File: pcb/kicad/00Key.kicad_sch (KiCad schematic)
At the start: 4 parts

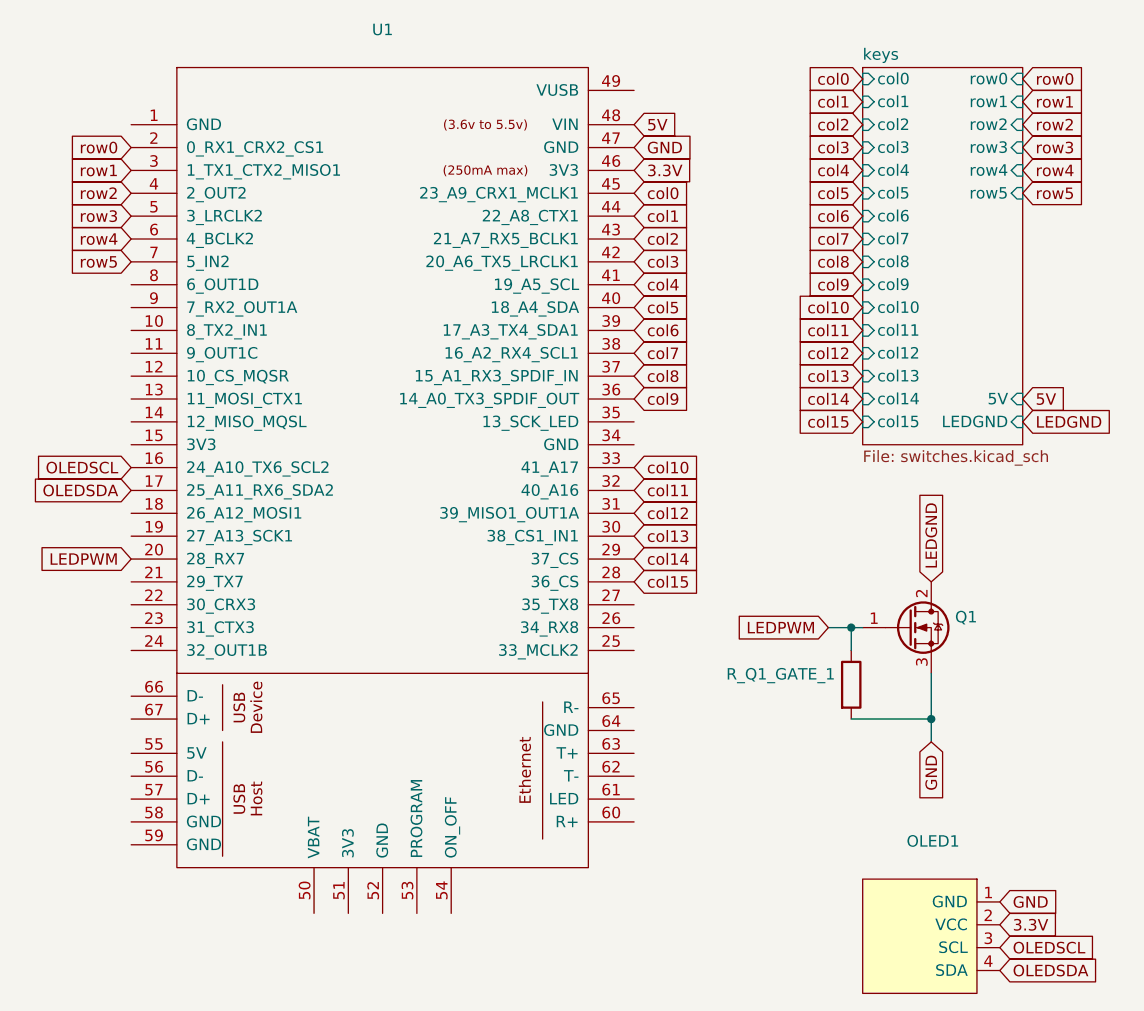
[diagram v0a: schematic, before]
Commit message: Modified schematic and pcb to use kailh hotswaps rather than MX+LED footprints
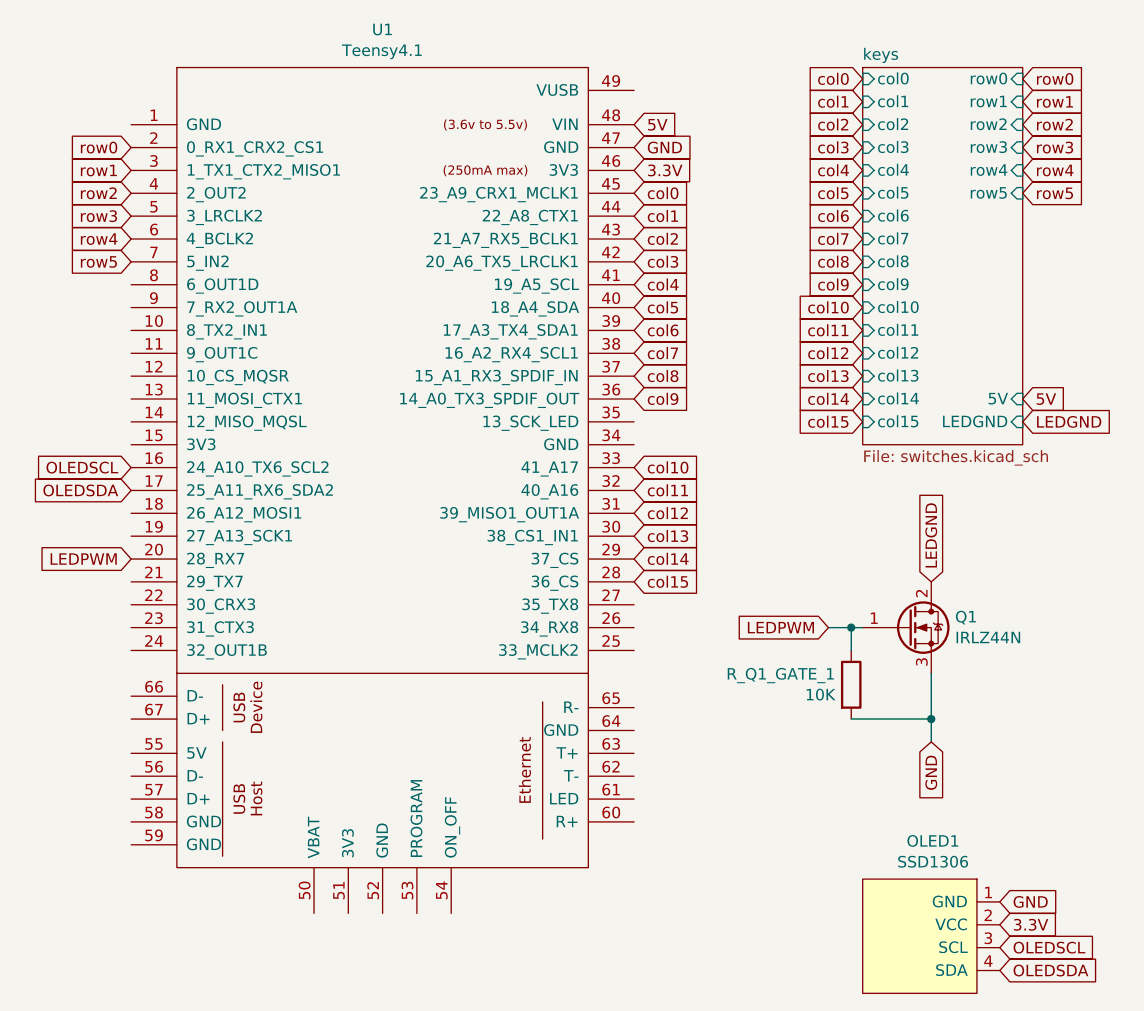
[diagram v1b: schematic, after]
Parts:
- OLED1: value (none) -> SSD1306; footprint (none) -> oled:128x64OLED
- Q1: value (none) -> IRLZ44N; footprint (none) -> Package_TO_SOT_THT:TO-220-3_Vertical
- R_Q1_GATE_1: value (none) -> 10K; footprint (none) -> Resistor_THT:R_Axial_DIN0207_L6.3mm_D2.5mm_P7.62mm_Horizontal
- U1: value (none) -> Teensy4.1; footprint (none) -> teensy:Teensy41

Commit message: Change diodes to smd, moved them to under switches, replaced teensy with header pins, reduced size of pcb
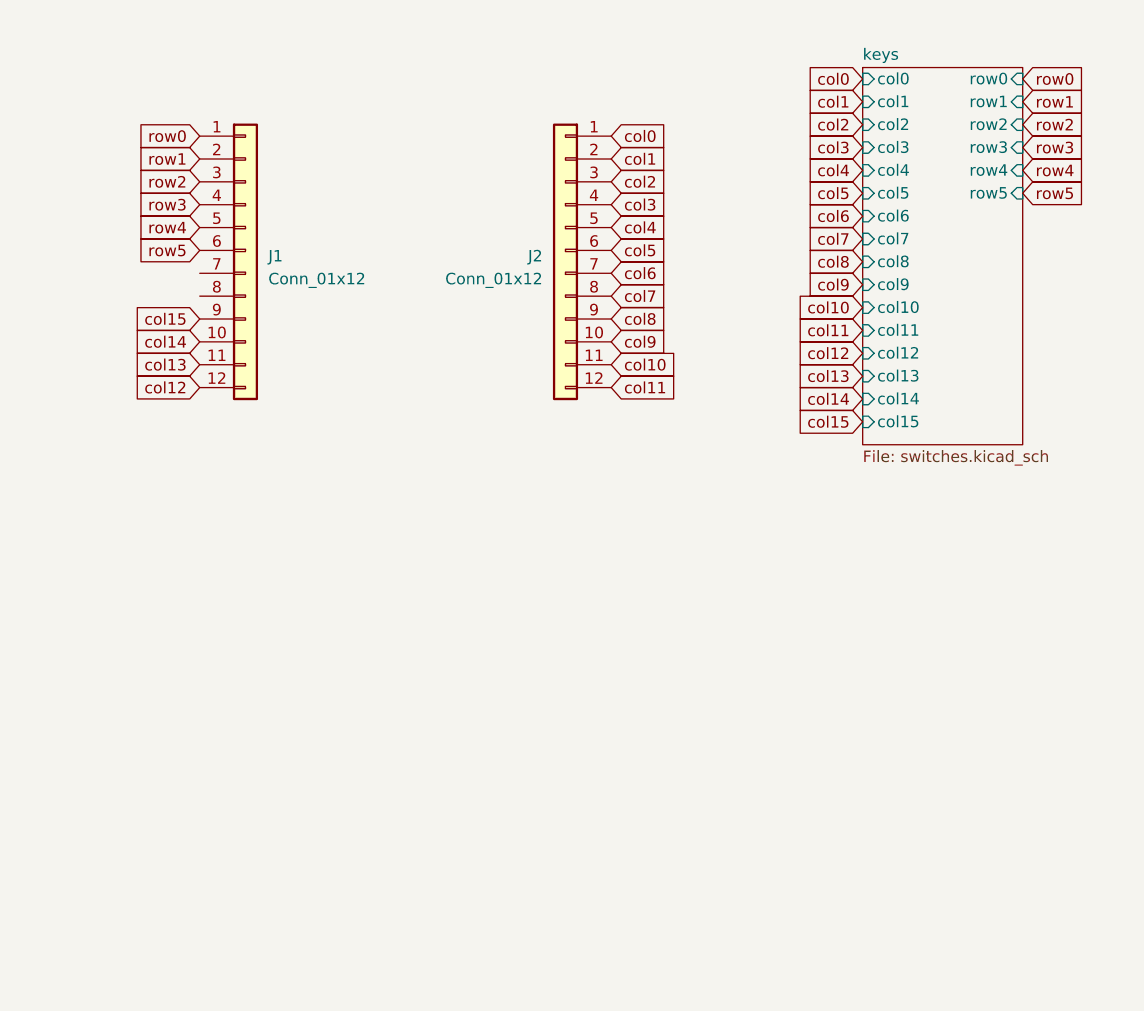
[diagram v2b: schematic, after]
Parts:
- removed OLED1: SSD1306, oled:128x64OLED, symbol 00Key-rescue:SSD1306-oled
- removed Q1: IRLZ44N, Package_TO_SOT_THT:TO-220-3_Vertical, symbol Transistor_FET:IRLZ44N
- removed R_Q1_GATE_1: 10K, Resistor_THT:R_Axial_DIN0207_L6.3mm_D2.5mm_P7.62mm_Horizontal, symbol Device:R
- removed U1: Teensy4.1, teensy:Teensy41, symbol 00Key-rescue:Teensy4.1-teensy
- added J1, J2: Conn_01x12, Connector_PinSocket_2.54mm:PinSocket_1x12_P2.54mm_Horizontal, symbol Connector_Generic:Conn_01x12
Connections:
- net col0: now also J2.1 (Pin_1)
- net col1: now also J2.2 (Pin_2)
- net col10: now also J2.11 (Pin_11)
- net col11: now also J2.12 (Pin_12)
- net col12: now also J1.12 (Pin_12)
- net col13: now also J1.11 (Pin_11)
- net col14: now also J1.10 (Pin_10)
- net col15: now also J1.9 (Pin_9)
- net col2: now also J2.3 (Pin_3)
- net col3: now also J2.4 (Pin_4)
- net col4: now also J2.5 (Pin_5)
- net col5: now also J2.6 (Pin_6)
- net col6: now also J2.7 (Pin_7)
- net col7: now also J2.8 (Pin_8)
- net col8: now also J2.9 (Pin_9)
- net col9: now also J2.10 (Pin_10)
- net row0: now also J1.1 (Pin_1)
- net row1: now also J1.2 (Pin_2)
- net row2: now also J1.3 (Pin_3)
- net row3: now also J1.4 (Pin_4)
- net row4: now also J1.5 (Pin_5)
- net row5: now also J1.6 (Pin_6)
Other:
- sheet keys ports: added none; removed 5V, LEDGND
